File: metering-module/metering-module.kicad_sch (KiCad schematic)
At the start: 39 parts, among them J1 North, J2 South, J3 West, J4 East, Q1 MMBT3904, Q2 MMBT3904, U1 LTV-817S, U2 LTV-817S, U3 BA033CC0FP-E2, U4 MAX3486, U5 MAX3486, U6 MCP23009-E_SS

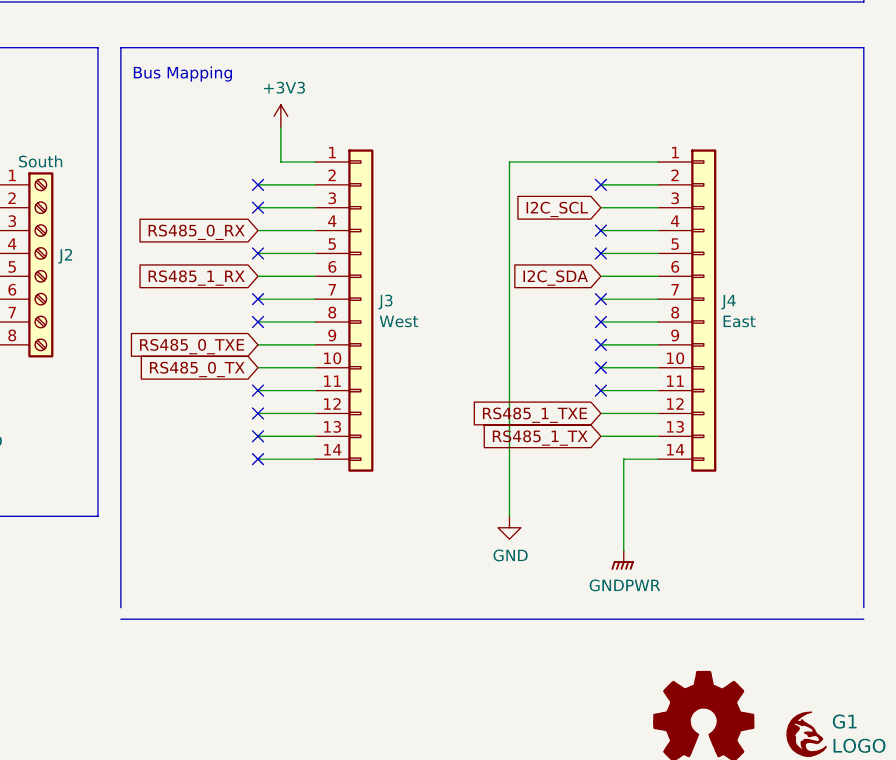
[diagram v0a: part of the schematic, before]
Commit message: Trim further warnings and errors
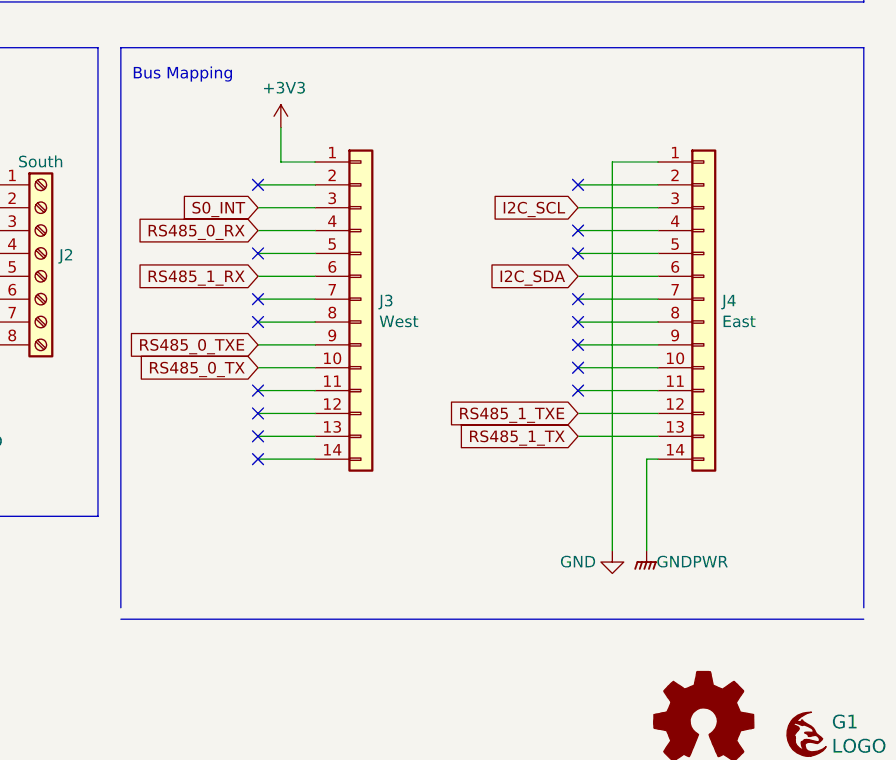
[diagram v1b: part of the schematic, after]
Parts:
- D2: footprint Diode_SMD:D_SOD-323_HandSoldering -> Diode_THT:D_DO-41_SOD81_P10.16mm_Horizontal
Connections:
- net S0_INT: now also J3.3 (Pin_3)
- no-connect marks 21 -> 20
